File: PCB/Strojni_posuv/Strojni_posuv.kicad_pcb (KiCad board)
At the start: 2 copper layers, 10 parts, among them IC1 TB6600HG, U1 STM32F103RBTx, U4 MIC5365-3.3YC5

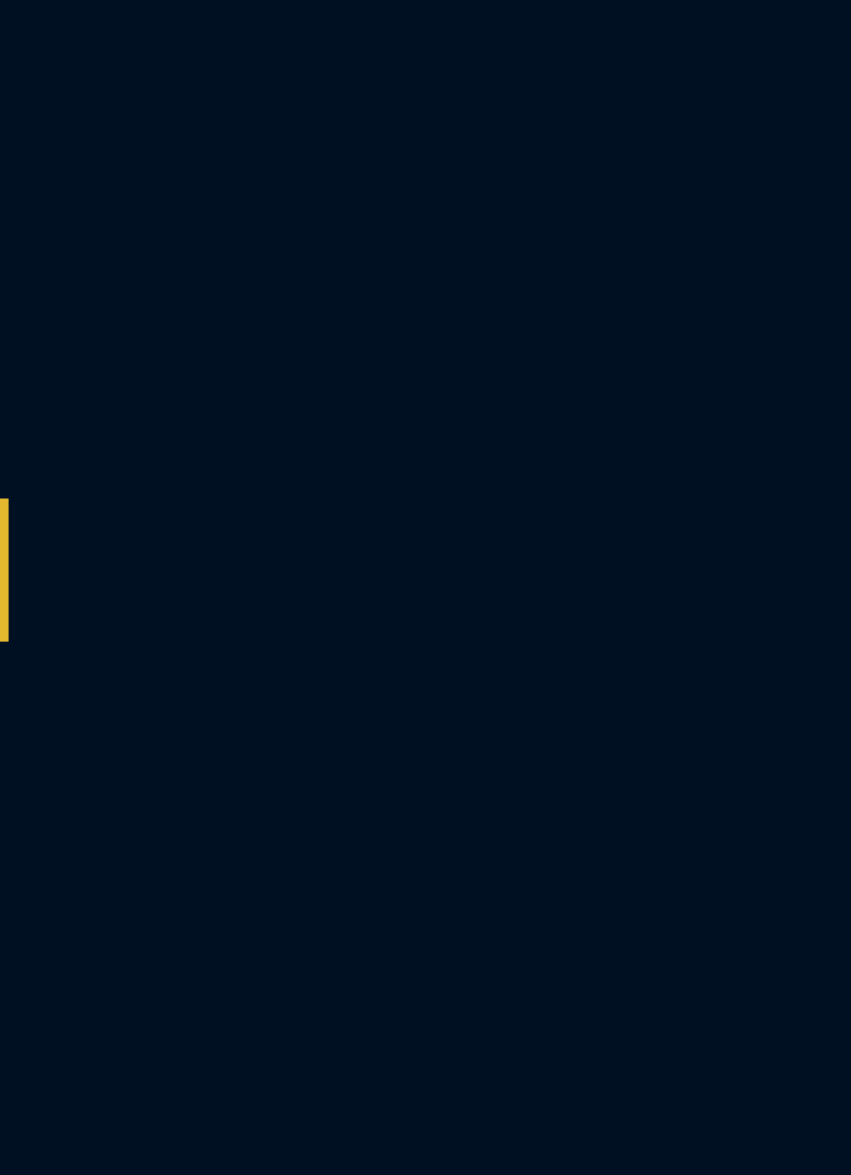
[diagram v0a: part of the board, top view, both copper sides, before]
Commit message: PCB making #3 Whole motor driver, small power changes, STM32 clock and new pin configuration
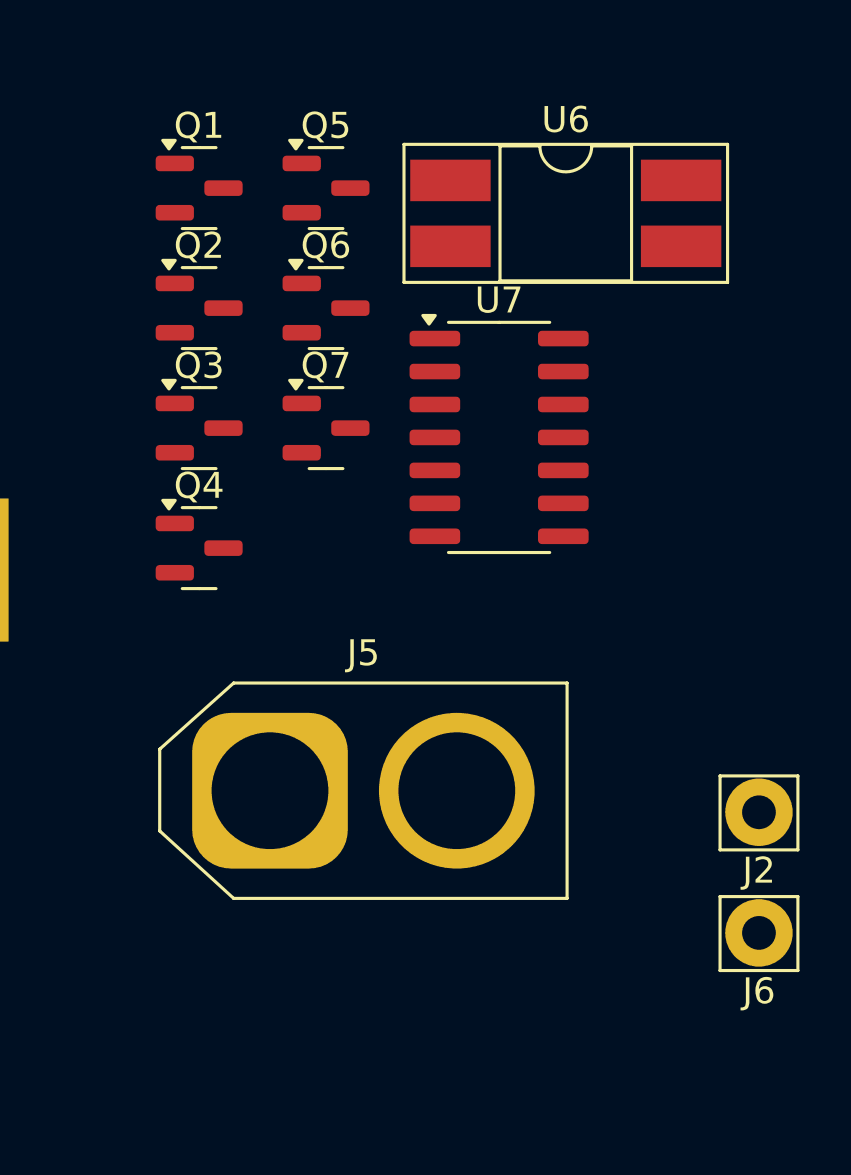
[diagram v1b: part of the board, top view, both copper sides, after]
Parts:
- added J2: Button_A, Connector_Pin:Pin_D1.3mm_L11.3mm_W2.8mm_Flat, F.Cu at (128.5, 66.3)
- added J5: POWER, Connector_AMASS:AMASS_XT60-M_1x02_P7.20mm_Vertical, F.Cu at (109.7, 65.5)
- added J6: Button_A, Connector_Pin:Pin_D1.3mm_L11.3mm_W2.8mm_Flat, F.Cu at (128.5, 71.0)
- added Q1: BSS138, Package_TO_SOT_SMD:SOT-23, F.Cu at (106.9, 42.3)
- added Q2: BSS138, Package_TO_SOT_SMD:SOT-23, F.Cu at (106.9, 46.9)
- added Q3: BSS138, Package_TO_SOT_SMD:SOT-23, F.Cu at (106.9, 51.5)
- added Q4: BSS138, Package_TO_SOT_SMD:SOT-23, F.Cu at (106.9, 56.2)
- added Q5: BSS138, Package_TO_SOT_SMD:SOT-23, F.Cu at (111.8, 42.3)
- added Q6: BSS138, Package_TO_SOT_SMD:SOT-23, F.Cu at (111.8, 46.9)
- added Q7: BC847, Package_TO_SOT_SMD:SOT-23, F.Cu at (111.8, 51.5)
- added U6: PC817, Package_DIP:DIP-4_W8.89mm_SMDSocket_LongPads, F.Cu at (121.1, 43.3)
- added U7: 74HC14, Package_SO:SOIC-14_3.9x8.7mm_P1.27mm, F.Cu at (118.5, 51.9)
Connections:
- IC1 pad 1: unconnected-(IC1-ALERT-Pad1) -> Net-(IC1-ALERT)
- IC1 pad 10_1: unconnected-(IC1-OUT2B-Pad10_1) -> /Motor_driver/OUT2B
- IC1 pad 11: unconnected-(IC1-NFB-Pad11) -> Net-(IC1-NFB)
- IC1 pad 12_1: unconnected-(IC1-OUT1B-Pad12_1) -> /Motor_driver/OUT1B
- IC1 pad 13: unconnected-(IC1-PGNDB-Pad13) -> GND
- IC1 pad 14_1: unconnected-(IC1-OUT2A-Pad14_1) -> /Motor_driver/OUT2A
- IC1 pad 15: unconnected-(IC1-NFA-Pad15) -> Net-(IC1-NFA)
- IC1 pad 16_1: unconnected-(IC1-OUT1A-Pad16_1) -> /Motor_driver/OUT1A
- IC1 pad 17: unconnected-(IC1-PGNDA-Pad17) -> GND
- IC1 pad 18_1: unconnected-(IC1-ENABLE-Pad18_1) -> /Motor_driver/ENB
- IC1 pad 19: unconnected-(IC1-RESET-Pad19) -> +5V
- IC1 pad 20_1: unconnected-(IC1-VCC@1-Pad20_1) -> +48V
- IC1 pad 21: unconnected-(IC1-CLK-Pad21) -> /Motor_driver/CLK_L
- IC1 pad 22_1: unconnected-(IC1-CW/CCW-Pad22_1) -> /Motor_driver/DIR_L
- IC1 pad 23: unconnected-(IC1-OSC-Pad23) -> Net-(IC1-OSC)
- IC1 pad 24_1: unconnected-(IC1-VREG-Pad24_1) -> Net-(IC1-VREG)
- IC1 pad 2_1: unconnected-(IC1-SGND-Pad2_1) -> GND
- IC1 pad 3: unconnected-(IC1-TQ-Pad3) -> /Motor_driver/TQ
- IC1 pad 4_1: unconnected-(IC1-LATCH/AUTO-Pad4_1) -> LTC
- IC1 pad 5: unconnected-(IC1-VREF-Pad5) -> Net-(IC1-VREF)
- IC1 pad 6_1: unconnected-(IC1-VCC-Pad6_1) -> +48V
- IC1 pad 7: unconnected-(IC1-M1-Pad7) -> M1
- IC1 pad 8_1: unconnected-(IC1-M2-Pad8_1) -> M2
- IC1 pad 9: unconnected-(IC1-M3-Pad9) -> M3
- U1 pad 2: unconnected-(U1-PC13-Pad2) -> LTC_STM
- U1 pad 29: DIR -> DIR_STM
- U1 pad 51: unconnected-(U1-PC10-Pad51) -> M1_STM
- U1 pad 52: unconnected-(U1-PC11-Pad52) -> M2_STM
- U1 pad 53: unconnected-(U1-PC12-Pad53) -> M3_STM
- U2 pad 3: 48V -> +48V

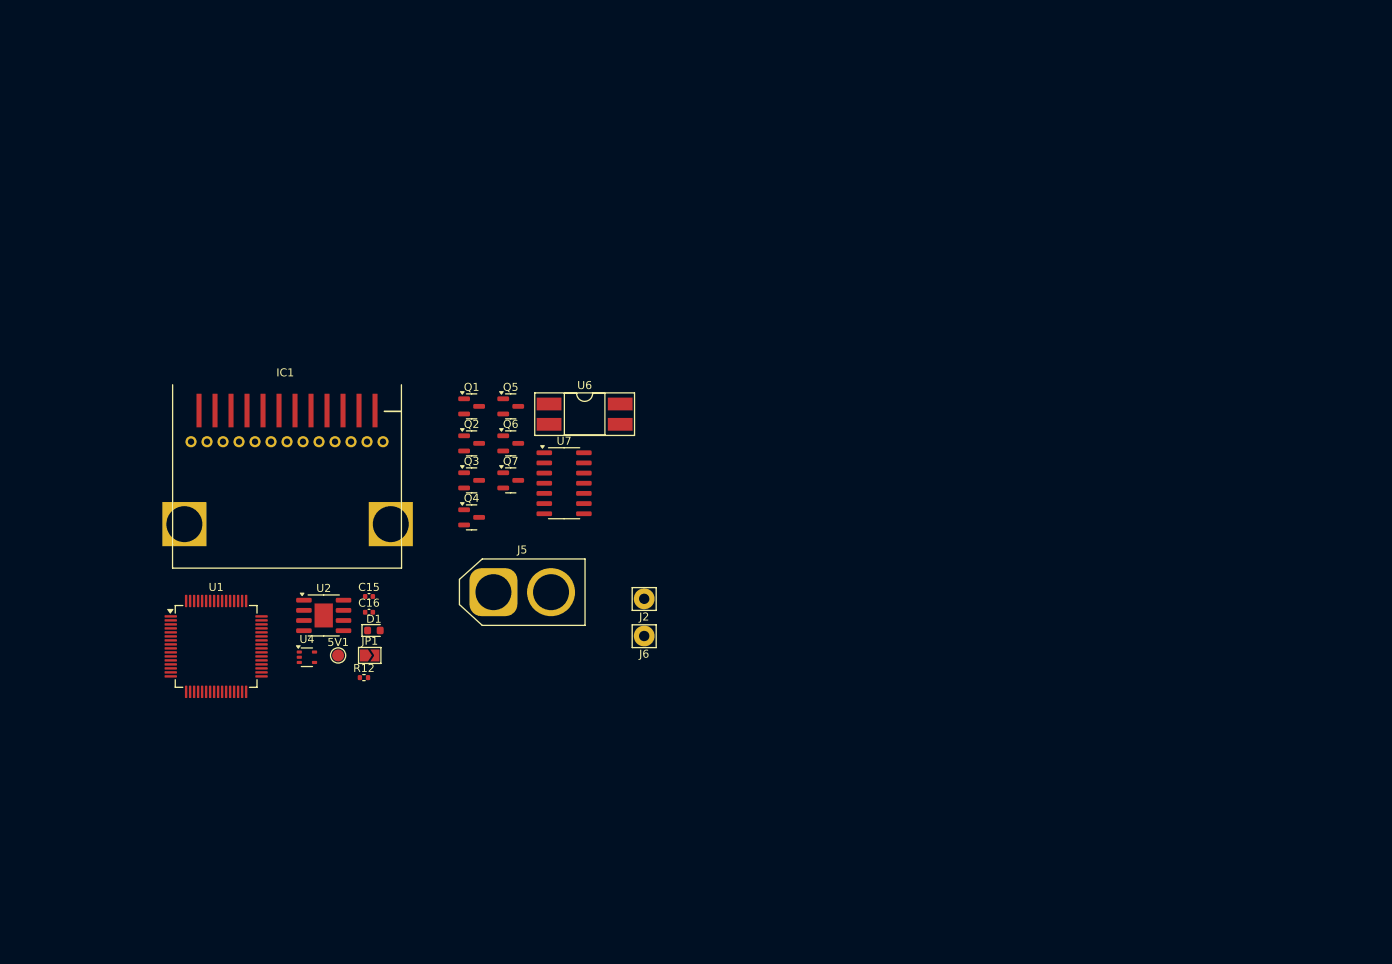
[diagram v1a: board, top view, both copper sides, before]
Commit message: PCB making #4 Finding components on JLCPCB and adding their tags to schematic. Assigning almost all footprints
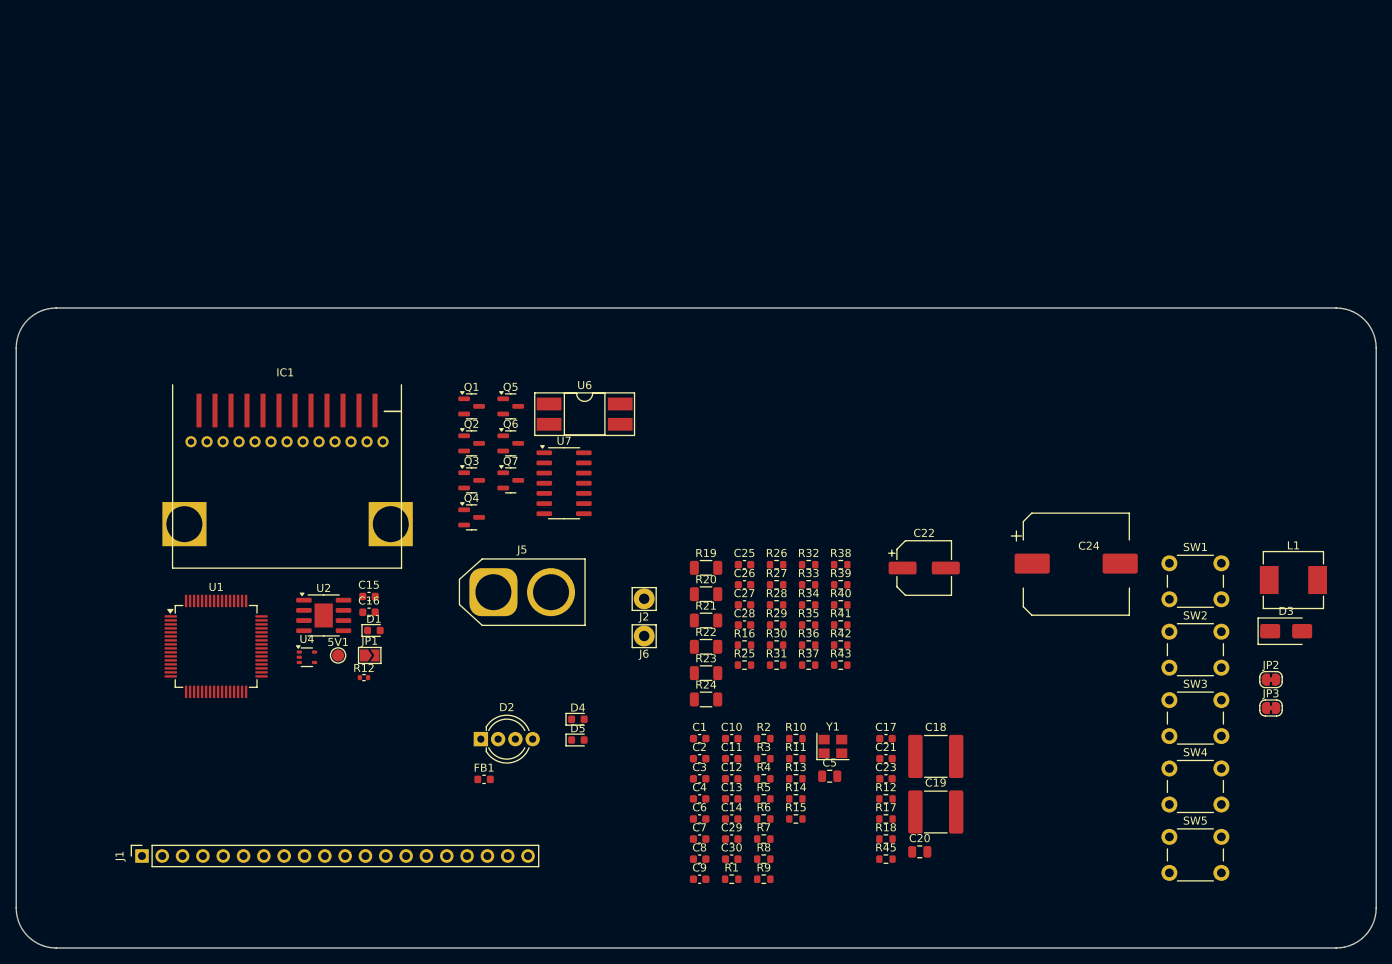
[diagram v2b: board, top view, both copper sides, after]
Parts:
- added C1: 100n, Capacitor_SMD:C_0603_1608Metric, F.Cu at (135.4, 83.8)
- added C10: 100n, Capacitor_SMD:C_0603_1608Metric, F.Cu at (139.4, 83.8)
- added C11: 100n, Capacitor_SMD:C_0603_1608Metric, F.Cu at (139.4, 86.3)
- added C12: 100n, Capacitor_SMD:C_0603_1608Metric, F.Cu at (139.4, 88.8)
- added C13: 100n, Capacitor_SMD:C_0603_1608Metric, F.Cu at (139.4, 91.4)
- added C14: 100n, Capacitor_SMD:C_0603_1608Metric, F.Cu at (139.4, 93.9)
- added C17: 100n, Capacitor_SMD:C_0603_1608Metric, F.Cu at (158.7, 83.8)
- added C18: 22u, Capacitor_SMD:C_2220_5750Metric, F.Cu at (164.9, 86.0)
- added C19: 22u, Capacitor_SMD:C_2220_5750Metric, F.Cu at (164.9, 93.0)
- added C2: 100n, Capacitor_SMD:C_0603_1608Metric, F.Cu at (135.4, 86.3)
- added C20: 2.2u, Capacitor_SMD:C_0805_2012Metric, F.Cu at (162.9, 98.0)
- added C21: 100n, Capacitor_SMD:C_0603_1608Metric, F.Cu at (158.7, 86.3)
- added C22: 470uF-6.3V, Capacitor_SMD:CP_Elec_6.3x7.7, F.Cu at (163.5, 62.5)
- added C23: 100n, Capacitor_SMD:C_0603_1608Metric, F.Cu at (158.7, 88.8)
- added C24: 470uF-50V, StuffBench:CP_Elec_12.5x16, F.Cu at (184.8, 62.0)
- added C25: 100n, Capacitor_SMD:C_0603_1608Metric, F.Cu at (141.0, 62.1)
- added C26: 100n, Capacitor_SMD:C_0603_1608Metric, F.Cu at (141.0, 64.6)
- added C27: 100n, Capacitor_SMD:C_0603_1608Metric, F.Cu at (141.0, 67.1)
- added C28: 100n, Capacitor_SMD:C_0603_1608Metric, F.Cu at (141.0, 69.6)
- added C29: 10p, Capacitor_SMD:C_0603_1608Metric, F.Cu at (139.4, 96.4)
- added C3: 100n, Capacitor_SMD:C_0603_1608Metric, F.Cu at (135.4, 88.8)
- added C30: 10p, Capacitor_SMD:C_0603_1608Metric, F.Cu at (139.4, 98.9)
- added C4: 100n, Capacitor_SMD:C_0603_1608Metric, F.Cu at (135.4, 91.4)
- added C5: 10u, Capacitor_SMD:C_0805_2012Metric, F.Cu at (151.7, 88.5)
- added C6: 10n, Capacitor_SMD:C_0603_1608Metric, F.Cu at (135.4, 93.9)
- added C7: 1u, Capacitor_SMD:C_0603_1608Metric, F.Cu at (135.4, 96.4)
- added C8: 1u, Capacitor_SMD:C_0603_1608Metric, F.Cu at (135.4, 98.9)
- added C9: 100n, Capacitor_SMD:C_0603_1608Metric, F.Cu at (135.4, 101.4)
- added D2: LED_RGBA, LED_THT:LED_D5.0mm-4_RGB_Wide_Pins, F.Cu at (108.1, 83.9)
- added D3: SS110, Diode_SMD:D_SMA, F.Cu at (208.7, 70.4)
- added D4: LED, LED_SMD:LED_0603_1608Metric, F.Cu at (120.2, 81.4)
- added D5: LED, LED_SMD:LED_0603_1608Metric, F.Cu at (120.2, 84.0)
- added FB1: FerriteBead, Inductor_SMD:L_0603_1608Metric, F.Cu at (108.5, 88.9)
- added J1: Conn_01x20_Pin, Connector_PinSocket_2.54mm:PinSocket_1x20_P2.54mm_Vertical, F.Cu at (65.7, 98.5)
- added JP2: SolderJumper_2_Bridged, Jumper:SolderJumper-2_P1.3mm_Bridged_RoundedPad1.0x1.5mm, F.Cu at (206.8, 76.5)
- added JP3: SolderJumper_2_Bridged, Jumper:SolderJumper-2_P1.3mm_Bridged_RoundedPad1.0x1.5mm, F.Cu at (206.8, 80.0)
- added L1: 33uH-2A, Inductor_SMD:L_Sunlord_MWSA0603S, F.Cu at (209.7, 64.0)
- added R1: 10K, Resistor_SMD:R_0603_1608Metric, F.Cu at (139.4, 101.4)
- added R10: 16.5K, Resistor_SMD:R_0603_1608Metric, F.Cu at (147.5, 83.8)
- added R11: 470, Resistor_SMD:R_0603_1608Metric, F.Cu at (147.5, 86.3)
- added R12: 470, Resistor_SMD:R_0603_1608Metric, F.Cu at (158.7, 91.4)
- added R13: 470, Resistor_SMD:R_0603_1608Metric, F.Cu at (147.5, 88.8)
- added R14: 470, Resistor_SMD:R_0603_1608Metric, F.Cu at (147.5, 91.4)
- added R15: 470, Resistor_SMD:R_0603_1608Metric, F.Cu at (147.5, 93.9)
- added R16: 470, Resistor_SMD:R_0603_1608Metric, F.Cu at (141.0, 72.1)
- added R17: 10K, Resistor_SMD:R_0603_1608Metric, F.Cu at (158.7, 93.9)
- added R18: 240K, Resistor_SMD:R_0603_1608Metric, F.Cu at (158.7, 96.4)
- added R19: 680m, Resistor_SMD:R_1206_3216Metric, F.Cu at (136.2, 62.5)
- added R2: 16.5K, Resistor_SMD:R_0603_1608Metric, F.Cu at (143.4, 83.8)
- added R20: 680m, Resistor_SMD:R_1206_3216Metric, F.Cu at (136.2, 65.8)
- added R21: 680m, Resistor_SMD:R_1206_3216Metric, F.Cu at (136.2, 69.1)
- added R22: 680m, Resistor_SMD:R_1206_3216Metric, F.Cu at (136.2, 72.3)
- added R23: 680m, Resistor_SMD:R_1206_3216Metric, F.Cu at (136.2, 75.6)
- added R24: 680m, Resistor_SMD:R_1206_3216Metric, F.Cu at (136.2, 78.9)
- added R25: 10K, Resistor_SMD:R_0603_1608Metric, F.Cu at (141.0, 74.6)
- added R26: 10K, Resistor_SMD:R_0603_1608Metric, F.Cu at (145.1, 62.1)
- added R27: 10K, Resistor_SMD:R_0603_1608Metric, F.Cu at (145.1, 64.6)
- added R28: 10K, Resistor_SMD:R_0603_1608Metric, F.Cu at (145.1, 67.1)
- added R29: 10K, Resistor_SMD:R_0603_1608Metric, F.Cu at (145.1, 69.6)
- added R3: 470, Resistor_SMD:R_0603_1608Metric, F.Cu at (143.4, 86.3)
- added R30: 10K, Resistor_SMD:R_0603_1608Metric, F.Cu at (145.1, 72.1)
- added R31: 10K, Resistor_SMD:R_0603_1608Metric, F.Cu at (145.1, 74.6)
- added R32: 10K, Resistor_SMD:R_0603_1608Metric, F.Cu at (149.1, 62.1)
- added R33: 470, Resistor_SMD:R_0603_1608Metric, F.Cu at (149.1, 64.6)
- added R34: 10K, Resistor_SMD:R_0603_1608Metric, F.Cu at (149.1, 67.1)
- added R35: 10K, Resistor_SMD:R_0603_1608Metric, F.Cu at (149.1, 69.6)
- added R36: 10K, Resistor_SMD:R_0603_1608Metric, F.Cu at (149.1, 72.1)
- added R37: 10K, Resistor_SMD:R_0603_1608Metric, F.Cu at (149.1, 74.6)
- added R38: 4.7K, Resistor_SMD:R_0603_1608Metric, F.Cu at (153.1, 62.1)
- added R39: 4.7K, Resistor_SMD:R_0603_1608Metric, F.Cu at (153.1, 64.6)
- added R4: 16.5K, Resistor_SMD:R_0603_1608Metric, F.Cu at (143.4, 88.8)
- added R40: 4.7K, Resistor_SMD:R_0603_1608Metric, F.Cu at (153.1, 67.1)
- added R41: 51K, Resistor_SMD:R_0603_1608Metric, F.Cu at (153.1, 69.6)
- added R42: 4.7K, Resistor_SMD:R_0603_1608Metric, F.Cu at (153.1, 72.1)
- added R43: 470, Resistor_SMD:R_0603_1608Metric, F.Cu at (153.1, 74.6)
- added R45: 470, Resistor_SMD:R_0603_1608Metric, F.Cu at (158.7, 98.9)
- added R5: 470, Resistor_SMD:R_0603_1608Metric, F.Cu at (143.4, 91.4)
- added R6: 16.5K, Resistor_SMD:R_0603_1608Metric, F.Cu at (143.4, 93.9)
- added R7: 16.5K, Resistor_SMD:R_0603_1608Metric, F.Cu at (143.4, 96.4)
- added R8: 470, Resistor_SMD:R_0603_1608Metric, F.Cu at (143.4, 98.9)
- added R9: 470, Resistor_SMD:R_0603_1608Metric, F.Cu at (143.4, 101.4)
- added SW1: SW_DPST_x2, Button_Switch_THT:SW_PUSH_6mm, F.Cu at (194.2, 61.9)
- added SW2: SW_DPST_x2, Button_Switch_THT:SW_PUSH_6mm, F.Cu at (194.2, 70.5)
- added SW3: SW_DPST_x2, Button_Switch_THT:SW_PUSH_6mm, F.Cu at (194.2, 79.0)
- added SW4: SW_DPST_x2, Button_Switch_THT:SW_PUSH_6mm, F.Cu at (194.2, 87.6)
- added SW5: SW_DPST_x2, Button_Switch_THT:SW_PUSH_6mm, F.Cu at (194.2, 96.1)
- added Y1: 16MHz, Crystal:Crystal_SMD_3225-4Pin_3.2x2.5mm, F.Cu at (152.1, 84.8)
- C15, C16: footprint Capacitor_SMD:C_0402_1005Metric -> Capacitor_SMD:C_0603_1608Metric
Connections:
- net STEP renamed STEP_STM
- U1 pad 12: unconnected-(U1-VSSA-Pad12) -> GND
- U1 pad 5: unconnected-(U1-PD0-Pad5) -> /RCC_OSC_IN
- U1 pad 6: unconnected-(U1-PD1-Pad6) -> /RCC_OSC_OUT
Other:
- board outline added: 170 x 80 mm

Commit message: PCB making #5 Starting with component placement
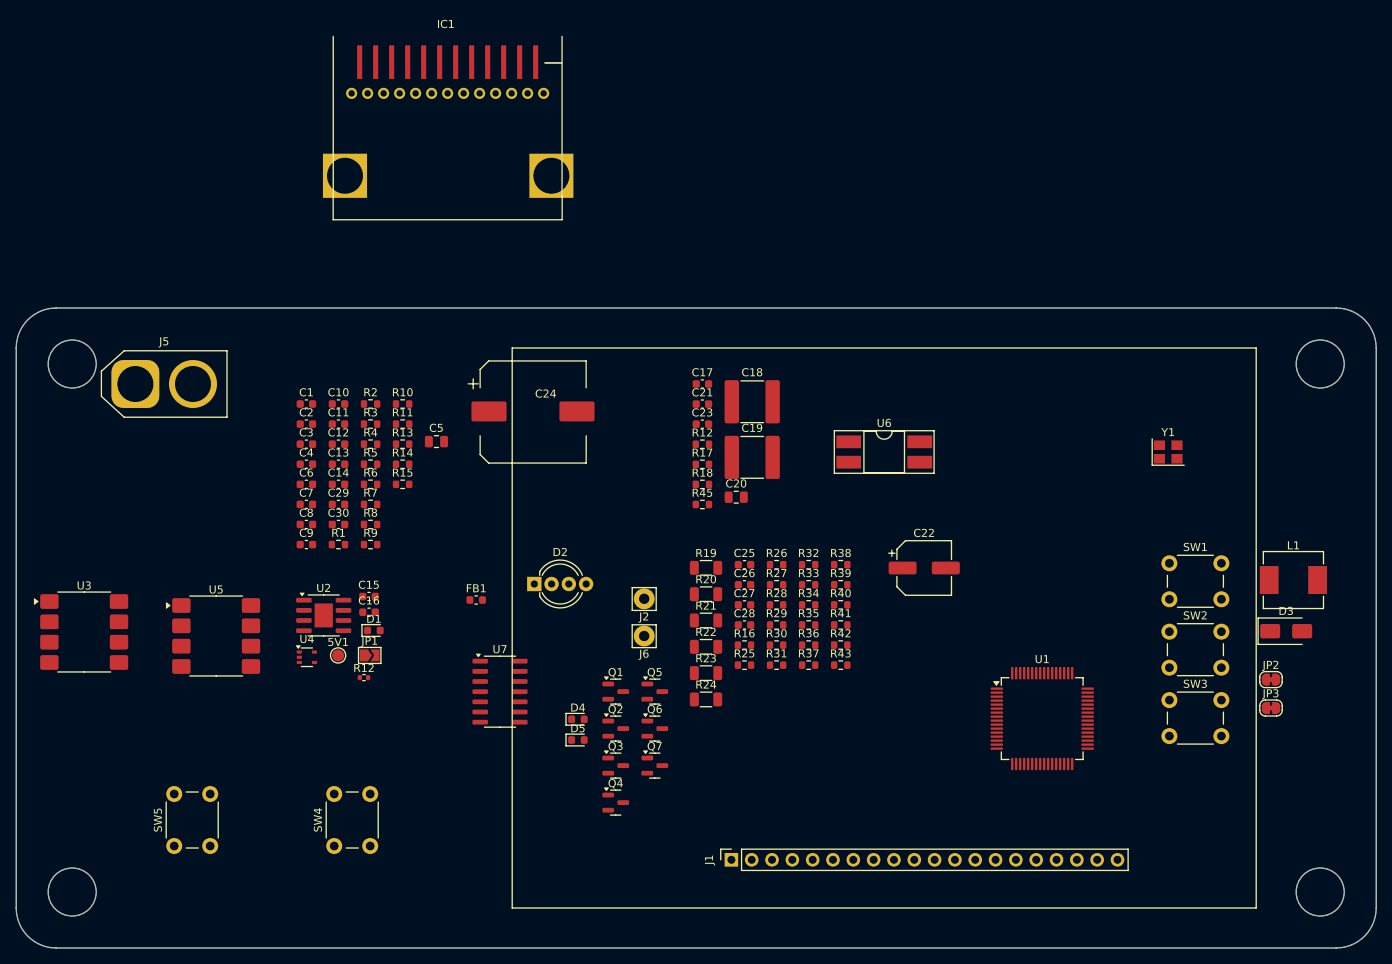
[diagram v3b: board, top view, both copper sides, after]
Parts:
- added U3: 6N137, Package_SO:SOP-8_6.605x9.655mm_P2.54mm, F.Cu at (58.5, 70.5)
- added U5: 6N137, Package_SO:SOP-8_6.605x9.655mm_P2.54mm, F.Cu at (75.0, 71.0)
- moved SW5 124.4 mm to (69.8, 97.2), turned to 90 degrees
- moved SW4 104.8 mm to (89.8, 97.2), turned to 90 degrees
- moved U1 103.7 mm to (178.2, 81.3)
- moved J1 73.7 mm to (139.4, 99.0)
- moved C24 70.5 mm to (116.9, 43.0)
- moved C11 64.5 mm to (90.3, 44.5)
- moved C14 64.5 mm to (90.3, 52.0)
- moved C2 64.5 mm to (86.3, 44.5)
- moved C6 64.5 mm to (86.3, 52.0)
- moved C9 64.5 mm to (86.3, 59.6)
- moved R1 64.5 mm to (90.3, 59.6)
- moved R11 64.5 mm to (98.3, 44.5)
- moved R15 64.5 mm to (98.3, 52.0)
- moved C1 64.5 mm to (86.3, 42.0)
- moved C10 64.5 mm to (90.3, 42.0)
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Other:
- outline, holes or cut-outs redrawn
